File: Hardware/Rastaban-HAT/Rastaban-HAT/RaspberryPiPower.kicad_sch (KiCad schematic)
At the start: 19 parts, among them IC2 BCM53DS, Q3 DMG2305UX-7, U5 RT7272AGSP

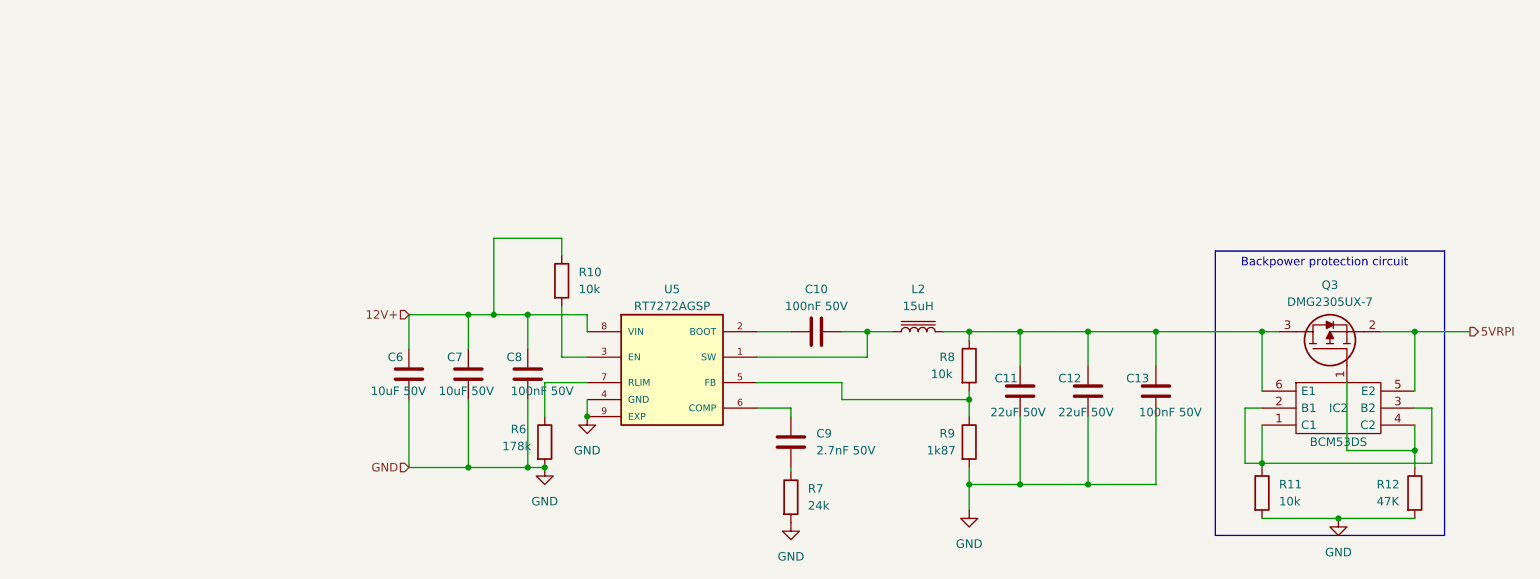
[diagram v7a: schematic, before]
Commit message: Started on V0.2 PCB and V1.3 schematic
-added new power circuit for RPI (removed old one rt7272)
-made daughter schematics sheets smaller
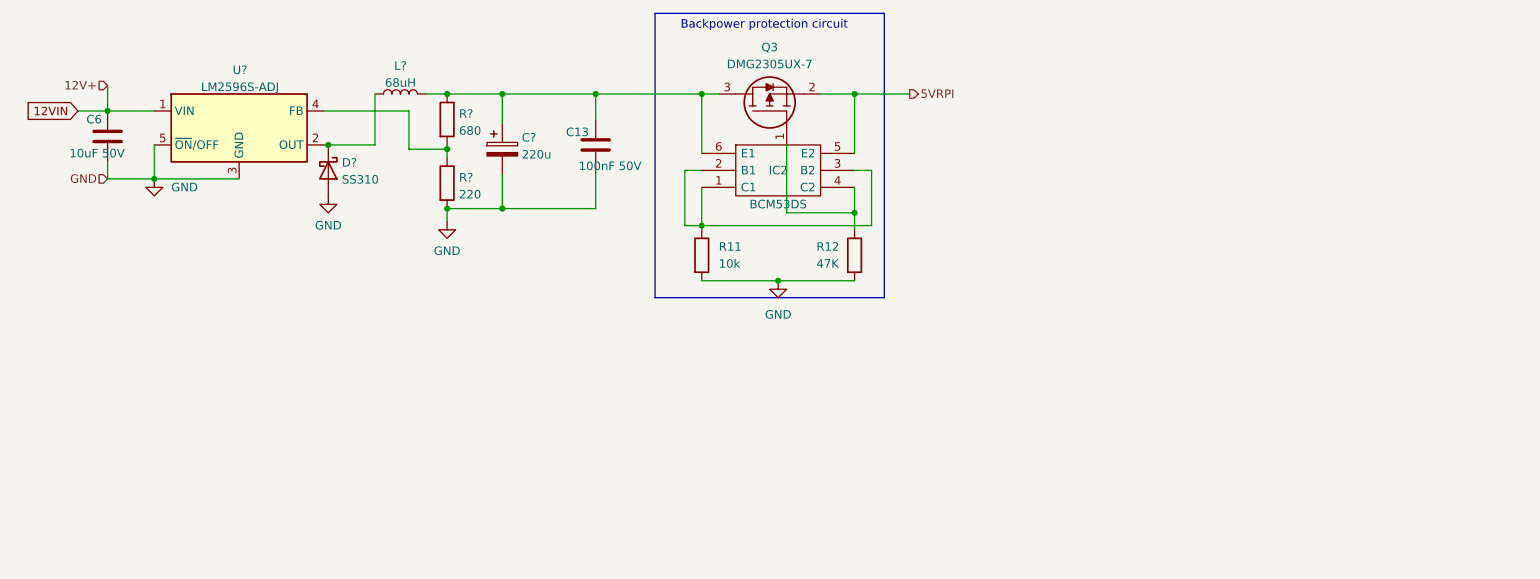
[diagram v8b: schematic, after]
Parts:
- removed C10, C8: 100nF 50V, Capacitor_SMD:C_0805_2012Metric_Pad1.18x1.45mm_HandSolder, symbol Device:C
- removed C11, C12: 22uF 50V, Capacitor_SMD:CP_Elec_6.3x5.8, symbol Device:C
- removed C7: 10uF 50V, Capacitor_SMD:C_0805_2012Metric_Pad1.18x1.45mm_HandSolder, symbol Device:C
- removed C9: 2.7nF 50V, Capacitor_SMD:C_0805_2012Metric_Pad1.18x1.45mm_HandSolder, symbol Device:C
- removed L2: 15uH, Inductor_SMD:L_1206_3216Metric_Pad1.22x1.90mm_HandSolder, symbol Device:L_Iron
- removed R10, R8: 10k, Resistor_SMD:R_0805_2012Metric_Pad1.20x1.40mm_HandSolder, symbol Device:R
- removed R6: 178k, Resistor_SMD:R_0805_2012Metric_Pad1.20x1.40mm_HandSolder, symbol Device:R
- removed R7: 24k, Resistor_SMD:R_0805_2012Metric_Pad1.20x1.40mm_HandSolder, symbol Device:R
- removed R9: 1k87, Resistor_SMD:R_0805_2012Metric_Pad1.20x1.40mm_HandSolder, symbol Device:R
- removed U5: RT7272AGSP, SnapEDA Library:SOIC127P599X175-9N, symbol RT7272AGSP:RT7272AGSP
- added C?: 220u, Capacitor_SMD:C_0603_1608Metric_Pad1.08x0.95mm_HandSolder, symbol Device:C_Polarized
- added D?: SS310, symbol Device:D_Schottky
- added L?: 68uH, Inductor_SMD:L_Bourns-SRU8028_8.0x8.0mm, symbol Device:L
- added R?: 220, Resistor_SMD:R_0603_1608Metric_Pad0.98x0.95mm_HandSolder, symbol Device:R
- added R?: 680, Resistor_SMD:R_0603_1608Metric_Pad0.98x0.95mm_HandSolder, symbol Device:R
- added U?: LM2596S-ADJ, Package_TO_SOT_SMD:TO-263-5_TabPin3, symbol Regulator_Switching:LM2596S-ADJ
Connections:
- net GND: now also C?.2, D?.2 (A), R?.2, U?.3 (GND), U?.5 (~{ON}/OFF)
- net at C13.2, IC2.6 (E1), Q3.3: now also C?.1, L?.2, R?.1
- net 12V+ renamed 12VIN
- net 12VIN: now also U?.1 (VIN)
- new net: D?.1 (K), L?.1, U?.2 (OUT)
- new net: R?.1, R?.2, U?.4 (FB)
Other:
- moved on the sheet: C13, C6, IC2, Q3, R11, R12
